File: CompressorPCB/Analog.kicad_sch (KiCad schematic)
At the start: 47 parts, among them Q1 NPN, Q2 PNP, Q3 PNP, U1 TL074, U2 TL074, U3 LM13700

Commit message: analog and power section schematics
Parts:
- removed Q1: NPN, symbol Simulation_SPICE:NPN
- removed Q2, Q3: PNP, symbol Simulation_SPICE:PNP
- added C3, C4: 100n, symbol Device:C
- added C7: 1u, symbol Device:C
- added Q1: BC847, Package_TO_SOT_SMD:SOT-23, symbol Transistor_BJT:BC847
- added Q2, Q3: BC857, Package_TO_SOT_SMD:SOT-23, symbol Transistor_BJT:BC857
- added R26: 22k, symbol Device:R_US
- added R29, R31: 47k, symbol Device:R_US
- added R33: 100R, symbol Device:R_US
- renumbered C3 to C1, C1 to C2, C4 to C5, C2 to C6, D4 to D3, D3 to D4, R20 to R10, R21 to R11, R6 to R12, R18 to R13, R19 to R14, R23 to R15, R5 to R16, R4 to R17, R24 to R18, R7 to R19, R13 to R2, R25 to R20, R26 to R21, R27 to R22, R8 to R23, R28 to R24, R32 to R25, R10 to R27, R9 to R28, R17 to R3, R12 to R30, R11 to R32, R29 to R34, R30 to R35, R31 to R36, R2 to R4, R3 to R5, R14 to R6, R15 to R7, R16 to R8, R22 to R9
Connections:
- net +18V: now also C3.2, C4.2
- net +9VA: now also R35.1, R26.2, R29.1
- net GND: now also C3.1, C4.1
- net Iabc: now also Q3.3 (C)
- net VG: no longer R35.1
- net at R25.1: now also R26.1
- net at R25.2: now also U2.3 (+)
- net at R36.1: now also Q3.2 (E)
- net at R34.1: now also Q2.2 (E)
- net at U2.8: now also Q1.1 (B)
- net at R35.2, U2.9 (-): now also Q1.2 (E)
- net OUT_BIASED: now reaches U2.1
- net OUT_BIASED: now also C7.1, R31.2
- net at U2.2 (-): now also R29.2, R31.1
- net VCAout: no longer names the net of C5.1, R21.1, U3.9
- new net: Q1.3 (C), Q2.1 (B), Q2.3 (C), Q3.1 (B)
- new net: C7.2, R33.1
- new net FX_OUT: R33.2
- no-connect marks 11 -> 8
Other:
- note added: "Control current source"
- note added: "Envelope follower"
- note added: "Ratio and threshold controls"
- note added: "VCA"
- moved on the sheet: C1, C2, C5, C6, D1, D2, D3, D4, D5, R1, R10, R11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

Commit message: ADC driver dialed in
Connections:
- net OUT_BIASED: now also C5.2, R25.3; no longer C7.1, R31.2, U2.1
- new net: C7.1, R31.2, U2.1

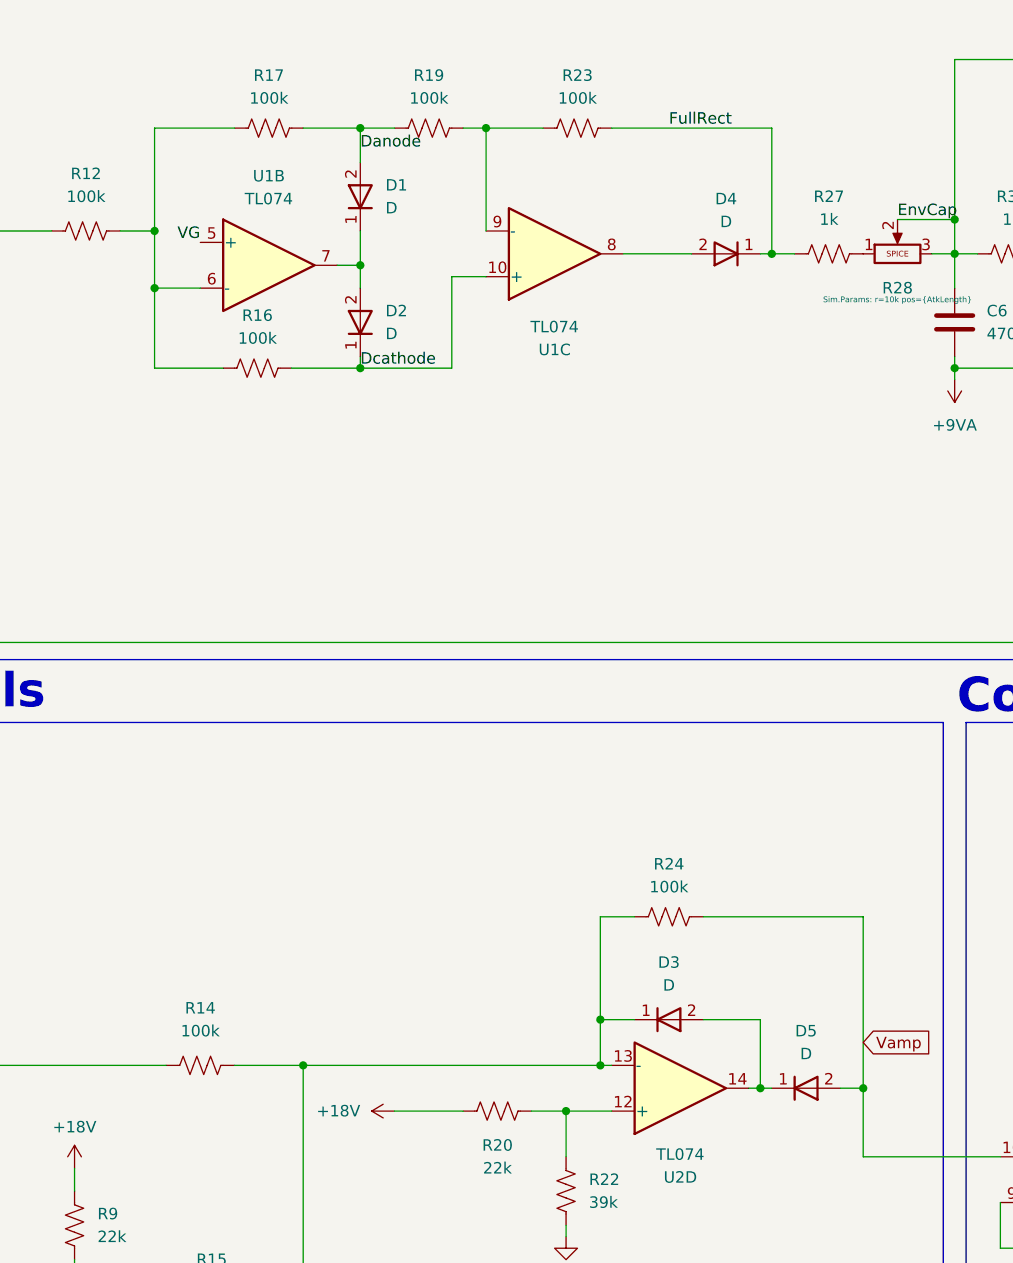
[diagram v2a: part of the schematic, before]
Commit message: schematic labels, footprints chosen
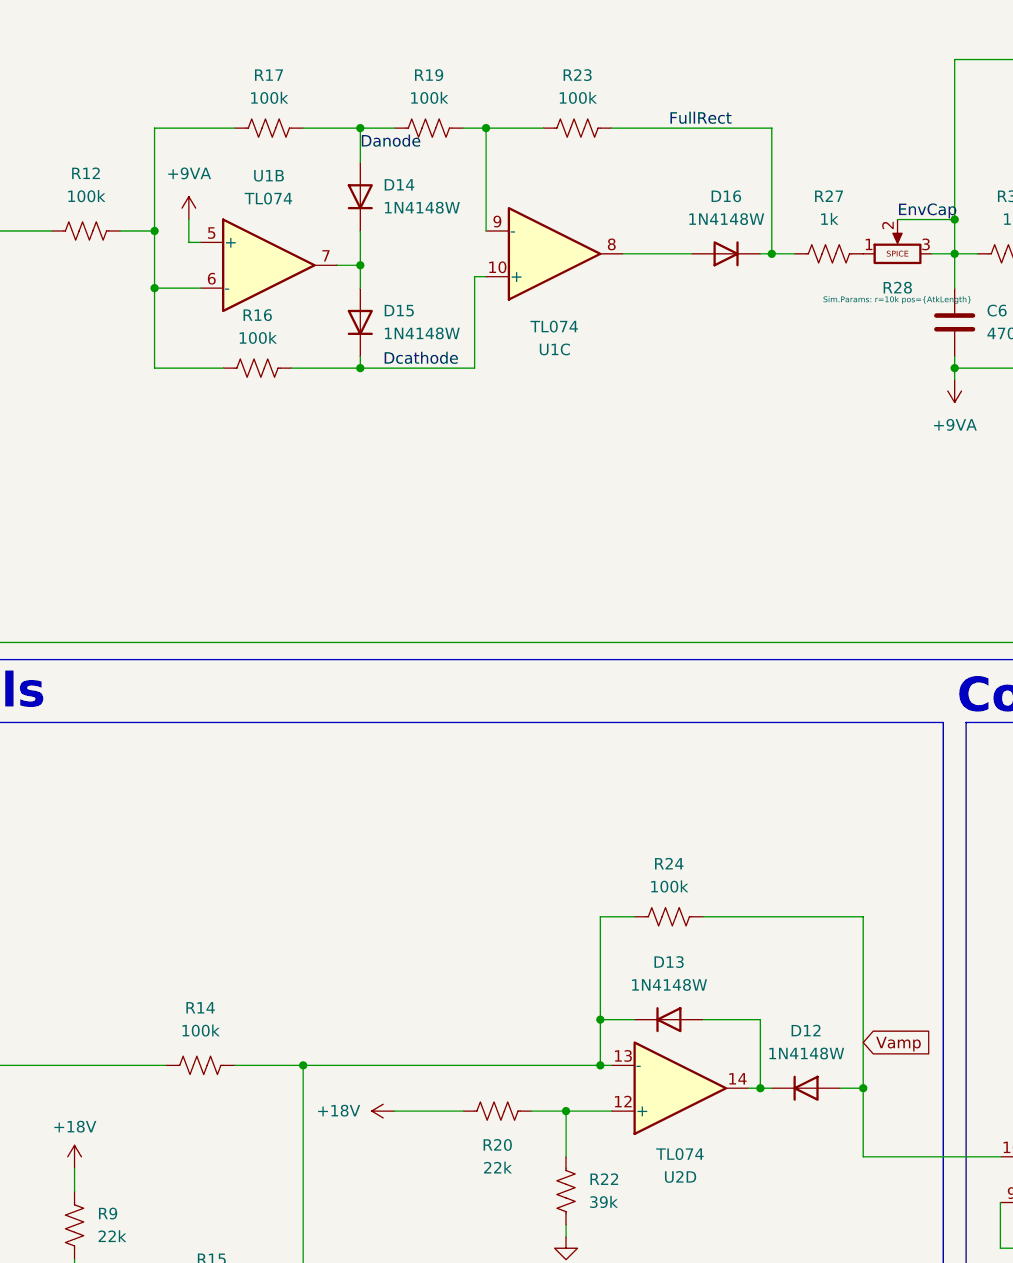
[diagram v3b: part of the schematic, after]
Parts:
- removed D1, D2, D3, D4, D5: D, symbol Simulation_SPICE:D
- added D12, D13, D14, D15, D16: 1N4148W, Diode_SMD:D_SOD-123, symbol Diode:1N4148W
- C1, C2, C3, C4, C5, C6, C7: footprint (none) -> Capacitor_SMD:C_0805_2012Metric
- R1, R11, R12, R13, R14, R15, R16, R17, R18, R19, R2, R20, R21, R22, R23, R24, R26, R27, R29, R3, R30, R31, R33, R34, R35, R36, R4, R5, R7, R8, R9: footprint (none) -> Resistor_SMD:R_0805_2012Metric
- R10, R25, R28, R32, R6: footprint (none) -> Potentiometer_THT:Potentiometer_Alpha_RV16AF_42_Single_Long
- U1, U2: footprint (none) -> Package_SO:SOIC-14_3.9x8.7mm_P1.27mm
- U3: footprint (none) -> Package_SO:SOIC-16_3.9x9.9mm_P1.27mm
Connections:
- net VG is gone; now on net +9VA: U1.5 (+)
- net Danode: now also D14.2 (A)
- net Dcathode: now also D15.1 (K)
- net FullRect: now also D16.1 (K)
- net Vamp: now also D12.2 (A)
- net at R14.2, R15.2, R24.1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: now also D13.1 (K)
- net at U1.8: now also D16.2 (A)
- net at U2.14: now also D12.1 (K), D13.2 (A)
- net at U1.7: now also D14.1 (K), D15.2 (A)

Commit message: basic layout
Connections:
- net +9VA: now also U1.3 (+); no longer U1.5 (+)
- net Dcathode: now also U1.5 (+); no longer U1.10 (+)
- net ENV: now also U1.8, U1.9 (-), U2.10 (+); no longer U1.13 (-), U1.14, U2.5 (+)
- net EnvCap: now also U1.10 (+); no longer U1.12 (+)
- net InAmp: now also U1.14; no longer U1.1
- net RatioAmp: now also U2.8; no longer U2.7
- net Vamp: now also U2.3 (+); no longer U2.10 (+)
- net at R29.2, R31.1: now also U2.6 (-); no longer U2.2 (-)
- net at C7.1, R31.2: now also U2.7; no longer U2.1
- net at R2.1, R3.1: now also U2.9 (-); no longer U2.6 (-)
- net at D14.1 (K), D15.2 (A): now also U1.1; no longer U1.7
- net at R4.1, R5.1: now also U1.13 (-); no longer U1.2 (-)
- net at C2.2, R1.1: now also U1.12 (+); no longer U1.3 (+)
- net at R12.2, R16.1, R17.1: now also U1.2 (-); no longer U1.6 (-)
- net at R19.2, R23.1: now also U1.6 (-); no longer U1.9 (-)
- net at R25.2: now also U2.5 (+); no longer U2.3 (+)
- net at D16.2 (A): now also U1.7; no longer U1.8
- net at Q1.1 (B): now also U2.1; no longer U2.8
- net at Q1.2 (E), R35.2: now also U2.2 (-); no longer U2.9 (-)
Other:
- moved on the sheet: U1A, U1B, U1C, U1D, U2A, U2B, U2C

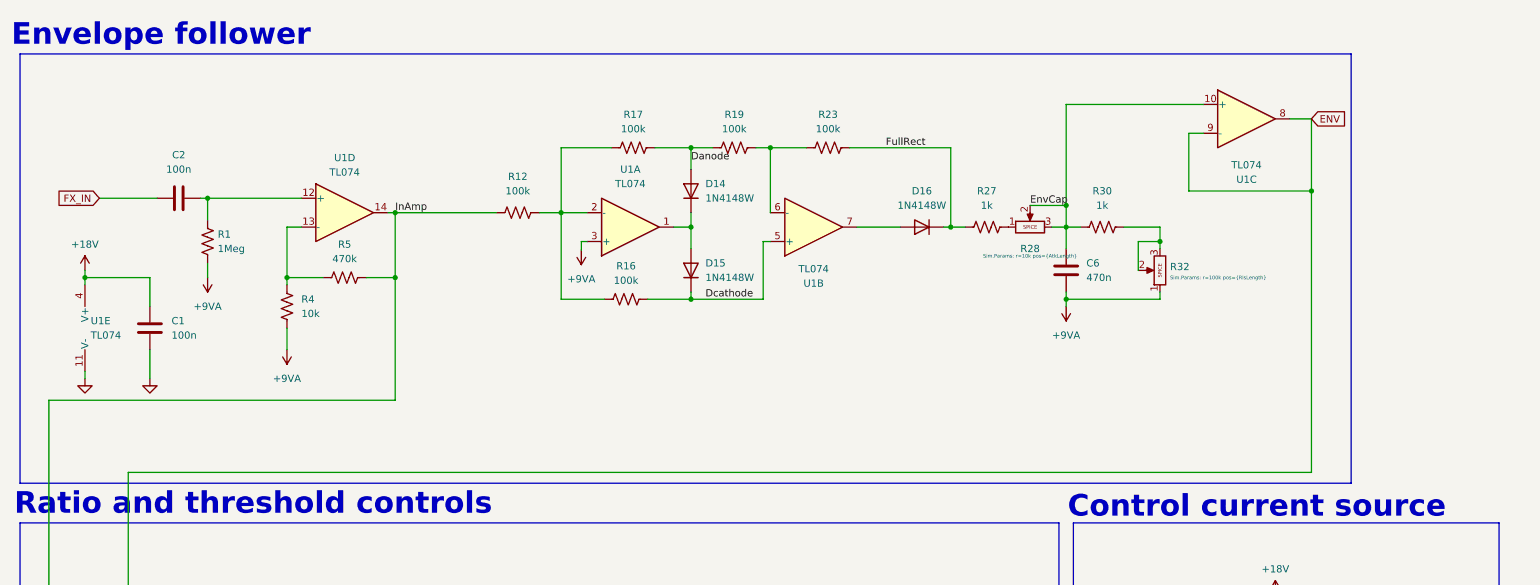
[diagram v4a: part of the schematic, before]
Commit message: updated env. follower and ADC driver in schem
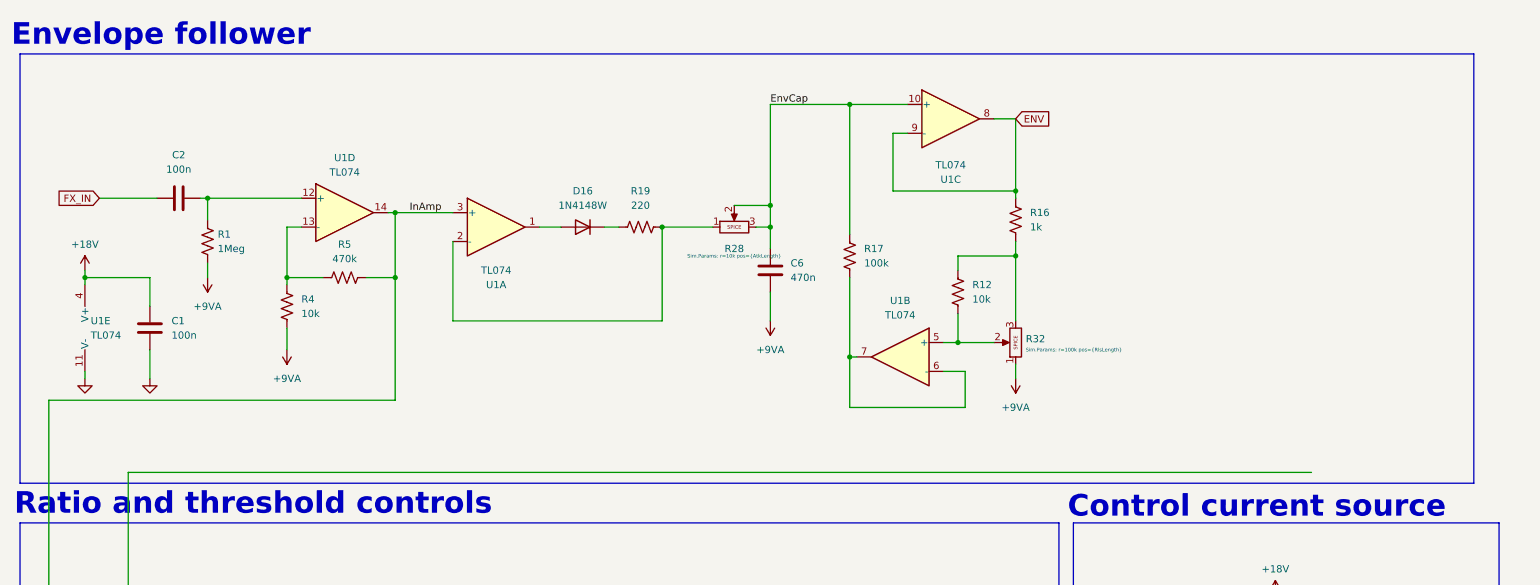
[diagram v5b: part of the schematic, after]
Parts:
- removed D14, D15: 1N4148W, Diode_SMD:D_SOD-123, symbol Diode:1N4148W
- removed R23: 100k, Resistor_SMD:R_0805_2012Metric, symbol Device:R_US
- removed R27, R30: 1k, Resistor_SMD:R_0805_2012Metric, symbol Device:R_US
- R12: value 100k -> 10k
- R16: value 100k -> 1k
- R19: value 100k -> 220
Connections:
- net FullRect is gone; now on an unnamed net: D16.1 (K)
- net +9VA: no longer U1.3 (+)
- net ENV: now also R16.1; no longer U2.10 (+)
- net EnvCap: now also R17.1
- net InAmp: now also U1.3 (+); no longer R12.1
- net at U1.1: now also D16.2 (A)
- net at R19.2: now also R28.1, U1.2 (-); no longer U1.6 (-)
- net at U1.7: now also R17.2, U1.6 (-); no longer D16.2 (A)
- net at R32.2: now also R12.2, U1.5 (+); no longer R32.3
- net Danode: no longer names the net of R19.1
- net Danode: no longer R17.2
- net Dcathode: no longer names the net of R16.2
- net Dcathode: now also R12.1, R32.3; no longer U1.5 (+)
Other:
- moved on the sheet: C6, D16, R28, R32, U1A, U1B, U1C

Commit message: routing start
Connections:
- net ENV: now also U1.6 (-), U1.7; no longer U1.8, U1.9 (-)
- net EnvCap: now also U1.5 (+); no longer U1.10 (+)
- net at R12.2, R32.2: now also U1.10 (+); no longer U1.5 (+)
- new net: R17.2, U1.8, U1.9 (-)
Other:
- moved on the sheet: U1B, U1C
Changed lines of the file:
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@@
 	(symbol
 		(lib_id "Amplifier_Operational:TL074")
-		(at 203.2 31.75 0)
+		(at 194.31 73.66 0)
+		(mirror y)
 		(unit 3)
 		(body_style 1)
@@
 		(in_pos_files yes)
 		(dnp no)
+		(fields_autoplaced yes)
 		(property "Reference" "U1"
-			(at 203.2 42.418 0)
+			(at 194.31 63.5 0)
 			(show_name no)
 			(do_not_autoplace no)
@@
 		)
 		(property "Value" "TL074"
-			(at 203.2 39.878 0)
+			(at 194.31 66.04 0)
 			(show_name no)
 			(do_not_autoplace no)
@@
 		)
 		(property "Footprint" "Package_SO:SOIC-14_3.9x8.7mm_P1.27mm"
-			(at 201.93 29.21 0)
+			(at 195.58 71.12 0)
 			(hide yes)
 			(show_name no)
@@
 		)
 		(property "Datasheet" "http://www.ti.com/lit/ds/symlink/tl071.pdf"
-			(at 204.47 26.67 0)
+			(at 193.04 68.58 0)
 			(hide yes)
 			(show_name no)
@@
 		)
 		(property "Description" "Quad Low-Noise JFET-Input Operational Amplifiers, DIP-14/SOIC-14"
-			(at 203.2 31.75 0)
+			(at 194.31 73.66 0)
 			(hide yes)
 			(show_name no)
@@
 		)
 		(property "Sim.Library" "/Users/hayden/dev/STM32_Projects/CompressorPedal/CompressorSim/tl074-quad.lib"
-			(at 203.2 31.75 0)
+			(at 194.31 73.66 0)
 			(hide yes)
 			(show_name no)
@@
 		)
 		(property "Sim.Name" "TL074c"
-			(at 203.2 31.75 0)
+			(at 194.31 73.66 0)
 			(hide yes)
 			(show_name no)
@@
 		)
 		(property "Sim.Device" "SUBCKT"
-			(at 203.2 31.75 0)
+			(at 194.31 73.66 0)
 			(hide yes)
 			(show_name no)
@@
 		)
 		(property "Sim.Pins" "1=1 2=2 3=3 4=4 5=5 6=6 7=7 8=8 9=9 10=10 11=11 12=12 13=13 14=14"
-			(at 203.2 31.75 0)
+			(at 194.31 73.66 0)
 			(hide yes)
 			(show_name no)
@@
 	(symbol
 		(lib_id "Amplifier_Operational:TL074")
-		(at 194.31 73.66 0)
-		(mirror y)
+		(at 203.2 31.75 0)
 		(unit 2)
 		(body_style 1)
@@
 		(in_pos_files yes)
 		(dnp no)
+		(fields_autoplaced yes)
 		(property "Reference" "U1"
-			(at 194.31 63.754 0)
+			(at 203.2 21.59 0)
 			(show_name no)
 			(do_not_autoplace no)
@@
 		)
 		(property "Value" "TL074"
-			(at 194.31 66.294 0)
+			(at 203.2 24.13 0)
 			(show_name no)
 			(do_not_autoplace no)
@@
 		)
 		(property "Footprint" "Package_SO:SOIC-14_3.9x8.7mm_P1.27mm"
-			(at 195.58 71.12 0)
+			(at 201.93 29.21 0)
 			(hide yes)
 			(show_name no)
@@
 		)
 		(property "Datasheet" "http://www.ti.com/lit/ds/symlink/tl071.pdf"
-			(at 193.04 68.58 0)
+			(at 204.47 26.67 0)
 			(hide yes)
 			(show_name no)
@@
 		)
 		(property "Description" "Quad Low-Noise JFET-Input Operational Amplifiers, DIP-14/SOIC-14"
-			(at 194.31 73.66 0)
+			(at 203.2 31.75 0)
 			(hide yes)
 			(show_name no)
@@
 		)
 		(property "Sim.Library" "/Users/hayden/dev/STM32_Projects/CompressorPedal/CompressorSim/tl074-quad.lib"
-			(at 194.31 73.66 0)
+			(at 203.2 31.75 0)
 			(hide yes)
 			(show_name no)
@@
 		)
 		(property "Sim.Name" "TL074c"
-			(at 194.31 73.66 0)
+			(at 203.2 31.75 0)
 			(hide yes)
 			(show_name no)
@@
 		)
 		(property "Sim.Device" "SUBCKT"
-			(at 194.31 73.66 0)
+			(at 203.2 31.75 0)
 			(hide yes)
 			(show_name no)
@@
 		)
 		(property "Sim.Pins" "1=1 2=2 3=3 4=4 5=5 6=6 7=7 8=8 9=9 10=10 11=11 12=12 13=13 14=14"
-			(at 194.31 73.66 0)
-			(hide yes)
-			(show_name no)
+			(at 203.2 31.75 0)
+			(hide yes)
+			(show_name no)

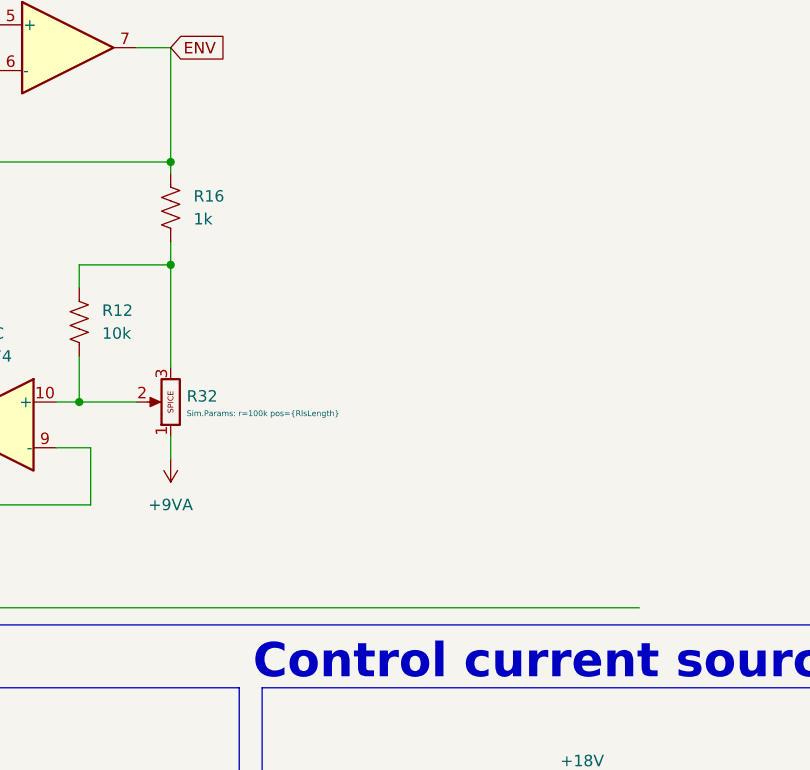
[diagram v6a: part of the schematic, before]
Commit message: all routed, DRC passing
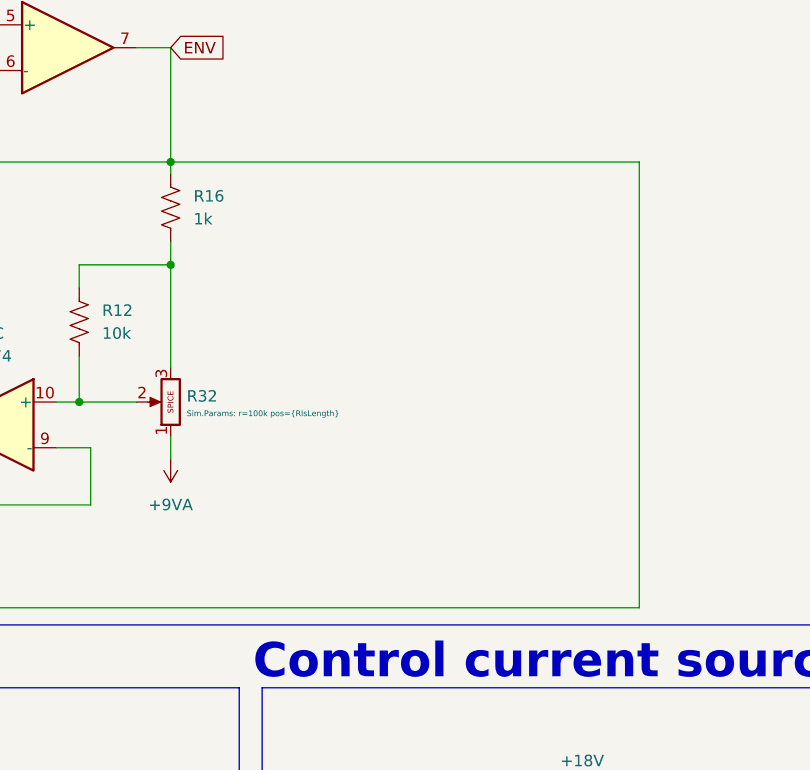
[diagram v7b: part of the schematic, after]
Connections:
- net ENV: now also U2.10 (+)
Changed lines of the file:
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@@
+	(wire
+		(pts
+			(xy 266.7 93.98) (xy 266.7 44.45)
+		)
+		(stroke
+			(width 0)
+			(type default)
+		)
+	)
 	(wire
 		(pts
@@
 		)
 		(stroke
+			(width 0)
+			(type default)
+		)
+	)
+	(wire
+		(pts
+			(xy 266.7 44.45) (xy 214.63 44.45)
+		)
+		(stroke
